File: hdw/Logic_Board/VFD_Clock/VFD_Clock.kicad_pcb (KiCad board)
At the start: 4 copper layers, 200 x 50 mm, 488 parts, among them J1601 Prog, J201 Power Input, J701 USB_B_Micro, Q1001 2N7002, Q1002 2N7002, Q1003 2N7002, Q1101 PMSTA06, Q1102 PMSTA06, Q1103 BC856W, Q1104 BC856W, Q1105 PMSTA06, Q1106 PMSTA06, Q1107 BC856W, Q1108 BC856W, Q1109 PMSTA06, Q1110 PMSTA06, Q1111 BC856W, Q1112 BC856W, Q1113 PMSTA06, Q1114 PMSTA06, Q1115 BC856W, Q1116 BC856W, Q1201 PMSTA06, Q1202 PMSTA06, Q1203 BC856W, Q1204 BC856W, Q1205 PMSTA06, Q1206 PMSTA06, Q1207 BC856W, Q1208 BC856W, Q1209 PMSTA06, Q1210 PMSTA06, Q1211 BC856W, Q1212 BC856W, Q1701 2N7002, Q201 Si2319CDS, Q202 PMT560ENEA, Q501 IRFL214TRPBF, SW1306 Select, U1001 TPS22929D, U1002 PCA9536DP, U1302 74LVC2G14, U1303 74LVC1G79, U1305 MAX6816, U1601 TL331, U1602 74LVC1G86, U1701 LTC3128-UFD, U1702 LTC4419DD, U1703 LTC3221, U1801 AT24CS01-STUM, U1901 74LVC1G38, U1902 74LVC1G38, U2001 OPT3001, U201 CDCS503, U202 LTC2946DE, U203 TPS2411PWR, U2101 MCP9700AT-HLT, U2102 MCP9700AT-HLT, U2103 MCP9700AT-HLT, U2104 MCP9700AT-HLT, U2201 74LVC1G08, U2202 DS1683, U2203 74LVC1G38, U2401 STWD100YNWWY3F, U2402 74LVC2G74, U301 PIC18LF67K40-I_PT, U401 LT8643S, U501 LT6700-1-S6, U502 LT3757, U601 TPS62150, U701 74LVC1G17, U702 TPD3S014DBVR, U703 FT234XD, U801 74LVC1G38, U802 74LVC1G38, U803 74LVC1G38, U804 74LVC1G38, U805 74LVC1G38, U806 74LVC1G240, U901 ISO7331C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

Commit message: Few fixes, added BLE
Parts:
- removed A1001: 0x41, Oddities:Dummy_Empty
- removed A1801: 0x50/0x58(UID), Oddities:Dummy_Empty
- removed A2001: 0x44, Oddities:Dummy_Empty
- removed A201: 0x6F, Oddities:Dummy_Empty
- removed A2201: 0x6B, Oddities:Dummy_Empty
- removed A301: MASTER, Oddities:Dummy_Empty
- removed BZ1001: AI-1027-TWT-3V-R, Custom Footprints Library:AI-1027-TWT-3V-R
- removed C1303, C1306, C1307, C1401, C1402, C1403, C1404, C1710, C1711, C305, C706, C707: 0.1uF, Capacitors_SMD:C_0603
- removed C1304, C1305, C1707: 2.2uF, Capacitors_SMD:C_0805
- removed C1708: 1uF, Capacitors_SMD:C_0603
- removed C1709: 4.7uF, Capacitors_SMD:C_0603
- removed C207: 2200pF, Capacitors_SMD:C_0603
- removed C208: 100pF, Capacitors_SMD:C_0603
- removed C209, C510: 47uF, Capacitors_Tantalum_SMD:CP_Tantalum_Case-X_EIA-7343-43_Reflow
- removed C2205, C2206: 10uF, Capacitors_SMD:C_1206
- removed C304, C307: 1nF, Capacitors_SMD:C_0603
- removed C306, C407, C710: 10nF, Capacitors_SMD:C_0603
- removed C308, C309: 9pF, Capacitors_SMD:C_0603
- removed C408: 1uF, Capacitors_SMD:C_0805
- removed C409: 4.7pF, Capacitors_SMD:C_0603
- removed C410: 100uF, Capacitors_SMD:C_1206
- removed C411: 220uF, Capacitors_Tantalum_SMD:CP_Tantalum_Case-X_EIA-7343-43_Reflow
- removed C506: 6.8nF, Capacitors_SMD:C_0603
- removed C507: 4.7uF, Capacitors_SMD:C_0805
- removed C508: 1uF, Capacitors_SMD:C_1210
- removed C509, C511: 0.1uF, Capacitors_SMD:C_0805
- removed C708, C709: 47pF, Capacitors_SMD:C_0603
- removed D1002: Orange, LEDs:LED_0603
- removed D1003, D1008, D1009, D806: Red, LEDs:LED_0603
- removed D1004, D1005, D1006: Blue, LEDs:LED_0603
- removed D1007, D801, D802, D803, D804, D805: Green, LEDs:LED_0603
- removed D1901, D1903: Green, LEDs:LED_D3.0mm_Horizontal_O3.81mm_Z10.0mm
- removed D1902, D1904: Green, LEDs:LED_D3.0mm_Horizontal_O1.27mm_Z2.0mm
- removed D2201: 1N5819, Diodes_SMD:D_SOD-123F
- removed D501: SMD1200PL-TP‎, Diodes_SMD:D_SOD-123
- removed D702: Yellow, LEDs:LED_0603
- removed F201: C1Q 2, Fuse_Holders_and_Fuses:Fuse_SMD1206_Reflow
- removed FB401: 100, Inductors_SMD:L_1812
- removed FID2301, FID2302, FID2303: TP, Fiducials:Fiducial_0.5mm_Dia_1mm_Outer
- removed G*** (x2): Microchip_Logo, Custom Footprints Library:Microchip_Logo
- removed J1601: Prog, Custom Footprints Library:PICKIT3_Header
- removed J701: USB_B_Micro, Connectors_USB:USB_Micro-B_Wuerth-629105150521_CircularHoles
- removed L501: 560uH, Inductors_SMD:L_Wuerth_WE-PD-Typ-LS
- removed L701: 600R 0.5A, Inductors_SMD:L_0603
- removed MH2301, MH2302, MH2303, MH2304, MH2305, MH2306, MH2307, MH2308: 4-40 Mounting Hole, Mounting_Holes:MountingHole_3mm
- removed MK2301, MK2302, MK2303, MK2304, MK2305, MK2306, MK2307, MK2308: #4-40 Screw, Oddities:Dummy_Empty
- removed MK2309, MK2310, MK2311, MK2312, MK2313, MK2314, MK2315, MK2316: #4-40 Standoff, Oddities:Dummy_Empty
- removed Q1002, Q1003, Q1701: 2N7002, TO_SOT_Packages_SMD:SOT-23
- removed Q1101, Q1102, Q1105, Q1106, Q1109, Q1110, Q1113, Q1114, Q1201, Q1202, Q1205, Q1206, Q1209, Q1210: PMSTA06, TO_SOT_Packages_SMD:SOT-323_SC-70
- removed Q1103, Q1104, Q1107, Q1108, Q1111, Q1112, Q1115, Q1116, Q1203, Q1204, Q1207, Q1208, Q1211, Q1212: BC856W, TO_SOT_Packages_SMD:SOT-323_SC-70
- removed Q501: IRFL214TRPBF, TO_SOT_Packages_SMD:SOT-223-3_TabPin2
- removed R1101, R1102, R1109, R1110, R1117, R1118, R1125, R1126, R1217, R1218, R1402, R1404, R1406, R1601, R1602, R1603, R1605, R1901, R1902, R1907, R1908, R2206, R303, R304, R305, R504, R506, R511, R701, R901, R902, R903, R904, R905, R906: 10k, Resistors_SMD:R_0603
- removed R1103, R1105, R1111, R1113, R1119, R1121, R1127, R1129, R1211, R1213, R1219, R1221: 220k, Resistors_SMD:R_0603
- removed R1104, R1106, R1112, R1114, R1120, R1122, R1128, R1130, R1212, R1214, R1220, R1222: 68k, Resistors_SMD:R_0603
- removed R1107, R1108, R1115, R1116, R1123, R1124, R1131, R1132, R1215, R1216, R1223, R1224, R1401, R1403, R1405, R1407: 100k, Resistors_SMD:R_0603
- removed R1408, R1903, R1904, R1905, R1906, R704, R811, R812: 1k, Resistors_SMD:R_0603
- removed R1604, R1708, R301, R302: 0, Resistors_SMD:R_0603
- removed R1706: 3.65k, Resistors_SMD:R_0603
- removed R1707: 340k, Resistors_SMD:R_0603
- removed R1709, R1712, R1713: 1M, Resistors_SMD:R_0603
- removed R1710: 324k, Resistors_SMD:R_0603
- removed R1711: 276k, Resistors_SMD:R_0603
- removed R501: 196k, Resistors_SMD:R_0603
- removed R502: 237, Resistors_SMD:R_0603
- removed R503: 1.2k, Resistors_SMD:R_0603
- removed R505: 10.5k, Resistors_SMD:R_0603
- removed R507: 22k, Resistors_SMD:R_0603
- removed R508: 2, Resistors_SMD:R_0603
- removed R509: 0.51, Resistors_SMD:R_1206
- removed R510: 356k, Resistors_SMD:R_0603
- removed R702, R703: 27, Resistors_SMD:R_0603
- removed REF**: Symbol_HighVoltage_Type2_Silkscreen_VerySmall, Custom Footprints Library:Symbol_HighVoltage_Type2_Silkscreen_VerySmall
- removed REF**: Symbol_Barrel_Polarity, Symbols:Symbol_Barrel_Polarity
- removed REF**: Symbol_Highvoltage_Type2_Silkscreen_Small, Custom Footprints Library:Symbol_Highvoltage_Type2_Silkscreen_Small
- removed REF***: KiCad-Logo_8mm_SilkScreen, Symbols:KiCad-Logo_8mm_SilkScreen
- removed REF***: OSHW-Logo2_14.6x12mm_SilkScreen, Symbols:OSHW-Logo2_14.6x12mm_SilkScreen
- removed REF***: ESD-Logo_13.2x12mm_SilkScreen, Symbols:ESD-Logo_13.2x12mm_SilkScreen
- removed SW1306: Select, Custom Footprints Library:ACZ11BR4E-15FA1-20C
- removed TP1301, TP1303: Date, Wire_Pads:SolderWirePad_single_SMD_5x10mm
- removed TP1302: Time, Wire_Pads:SolderWirePad_single_SMD_5x10mm
- removed TP1304: Alarm, Wire_Pads:SolderWirePad_single_SMD_5x10mm
- removed TP1305: Brightness, Wire_Pads:SolderWirePad_single_SMD_5x10mm
- removed TP1701, TP1702, TP501, TP701: TP, Measurement_Points:Measurement_Point_Round-SMD-Pad_Small
- removed TP301: I2C, Pin_Headers:Pin_Header_Straight_1x03_Pitch2.54mm
- removed TP302: USB_UART, Pin_Headers:Pin_Header_Straight_1x03_Pitch2.54mm
- removed TP702: TP, Pin_Headers:Pin_Header_Straight_1x01_Pitch2.54mm
- removed U1302: 74LVC2G14, TO_SOT_Packages_SMD:SOT-363_SC-70-6
- removed U1303: 74LVC1G79, TO_SOT_Packages_SMD:SOT-353_SC-70-5
- removed U1305: MAX6816, TO_SOT_Packages_SMD:SOT-143
- removed U1601: TL331, TO_SOT_Packages_SMD:SOT-23-5
- removed U1602: 74LVC1G86, TO_SOT_Packages_SMD:SOT-353_SC-70-5
- removed U1701: LTC3128-UFD, Housings_DFN_QFN:QFN-20-1EP_4x5mm_Pitch0.5mm
- removed U1702: LTC4419DD, Housings_DFN_QFN:DFN-10-1EP_3x3mm_Pitch0.5mm
- removed U1703: LTC3221, Housings_DFN_QFN:DFN-6-1EP_2x2mm_Pitch0.5mm
- removed U1902, U2203, U802, U803, U804, U805: 74LVC1G38, TO_SOT_Packages_SMD:SOT-353_SC-70-5
- removed U202: LTC2946DE, Housings_DFN_QFN:DFN-16-1EP_3x4mm_Pitch0.45mm
- removed U203: TPS2411PWR, Housings_SSOP:TSSOP-14_4.4x5mm_Pitch0.65mm
- removed U2202: DS1683, Housings_SOIC:SOIC-8_3.9x4.9mm_Pitch1.27mm
- removed U806: 74LVC1G240, TO_SOT_Packages_SMD:SOT-353_SC-70-5
- removed VFD0, VFD1, VFD2, VFD3, VFD4, VFD5: IV-6, VFD:IV-6
- removed Y301: 32.768kHz, Crystals:Crystal_SMD_2012-2pin_2.0x1.2mm
- removed Z1402, Z1403: BZT52C3V3S, Diodes_SMD:D_SOD-323
- removed Z1601: BZT52C5V6S, Diodes_SMD:D_SOD-323
- removed Z201: MMSZ5240BS, Diodes_SMD:D_SOD-323
- added BT1201: BR-2/3AE5SPN, Custom Footprints Library:BR-2_3AE5SPN, F.Cu at (326.2, 31.5)
- added BT1202: CR2032, Battery_Holders:Keystone_1058_1x2032-CoinCell, F.Cu at (362.1, 34.7)
- added BT1203: TLH-5935/P, Custom Footprints Library:TLH-5935, F.Cu at (342.5, 0.76)
- added BZ1801: CST-931RP-A, Buzzer_Beeper:MagneticBuzzer_CUI_CST-931RP-A, F.Cu at (432.5, 11.6)
- added C1003: 0.1uF, Capacitors_SMD:C_0603, F.Cu at (334.2, 82.3)
- added C1004: 0.1uF, Capacitors_SMD:C_0603, F.Cu at (319.2, 94.4)
- added C1005: 0.1uF, Capacitors_SMD:C_0603, F.Cu at (323.4, 92.7)
- added C1006: 10nF, Capacitors_SMD:C_0603, F.Cu at (319.2, 96.8)
- added C1007: 6.8nF, Capacitors_SMD:C_0603, F.Cu at (338.7, 79.5)
- added C1008: 1nF, Capacitors_SMD:C_0603, F.Cu at (327.5, 91.5)
- added C1009: 4.7uF, Capacitors_SMD:C_0805, F.Cu at (315.0, 96.3)
- added C1010: 1uF, Capacitors_SMD:C_1210, F.Cu at (329.5, 80.4)
- added C1011: 0.1uF, Capacitors_SMD:C_0805, F.Cu at (334.5, 79.8)
- added C1101: 0.1uF, Capacitors_SMD:C_0603, F.Cu at (449.8, 83.0)
- added C1102: 0.1uF, Capacitors_SMD:C_0603, F.Cu at (460.4, 78.3)
- added C1103: 0.1uF, Capacitors_SMD:C_0603, F.Cu at (460.0, 83.0)
- added C1104: 0.1uF, Capacitors_SMD:C_0603, F.Cu at (460.4, 80.6)
- added C1201: 10uF, Capacitors_SMD:C_1206, F.Cu at (310.0, 42.2)
- added C1202: 10uF, Capacitors_SMD:C_1206, F.Cu at (310.0, 48.6)
- added C1203: 10uF, Capacitors_SMD:C_1206, F.Cu at (315.5, 42.2)
- added C1204: 10uF, Capacitors_SMD:C_1206, F.Cu at (310.0, 45.3)
- added C1205: 0.1uF, Capacitors_SMD:C_0603, F.Cu at (381.0, 11.1)
- added C1206: 10uF, Capacitors_SMD:C_1206, F.Cu at (379.2, 8.38)
- added C1207: 10uF, Capacitors_SMD:C_1206, F.Cu at (315.5, 45.3)
- added C1501: 0.1uF, Capacitors_SMD:C_0603, F.Cu at (414.5, 181.9)
- added C1502: 0.1uF, Capacitors_SMD:C_0603, B.Cu at (420.0, 193.4)
- added C1604: 10nF, Capacitors_SMD:C_0603, F.Cu at (640.9, 148.3)
- added C1605: 10nF, Capacitors_SMD:C_0603, F.Cu at (645.2, 148.3)
- added C1606: 1nF, Capacitors_SMD:C_0603, F.Cu at (640.9, 146.9)
- added C1607: 1nF, Capacitors_SMD:C_0603, F.Cu at (645.2, 146.9)
- added C1608: 0.1uF, Capacitors_SMD:C_0603, F.Cu at (654.6, 130.4)
- added C1609: 0.1uF, Capacitors_SMD:C_0603, F.Cu at (643.7, 123.4)
- added C1610: 10uF, Capacitors_SMD:C_0603, F.Cu at (656.0, 130.4)
- added C1611: 10nF, Capacitors_SMD:C_0603, F.Cu at (653.2, 130.4)
- added C1612: 10nF, Capacitors_SMD:C_0603, F.Cu at (643.7, 124.8)
- added C1613: 1nF, Capacitors_SMD:C_0603, F.Cu at (651.8, 130.4)
- added C1614: 1nF, Capacitors_SMD:C_0603, F.Cu at (643.7, 126.2)
- added C1615: 0.1uF, Capacitors_SMD:C_0603, F.Cu at (639.3, 123.4)
- added C1616: 0.1uF, Capacitors_SMD:C_0603, F.Cu at (654.6, 136.8)
- added C1617: 10uF, Capacitors_SMD:C_0603, F.Cu at (639.3, 122.0)
- added C1618: 10nF, Capacitors_SMD:C_0603, F.Cu at (639.3, 124.8)
- added C1619: 10nF, Capacitors_SMD:C_0603, F.Cu at (653.2, 136.8)
- added C1620: 1nF, Capacitors_SMD:C_0603, F.Cu at (639.3, 126.2)
- added C1621: 1nF, Capacitors_SMD:C_0603, F.Cu at (651.8, 136.8)
- added C1622: 0.1uF, Capacitors_SMD:C_0603, F.Cu at (628.3, 136.9)
- added C1623: 0.1uF, Capacitors_SMD:C_0603, F.Cu at (637.7, 149.7)
- added C1624: 10uF, Capacitors_SMD:C_0603, F.Cu at (626.9, 136.9)
- added C1625: 10nF, Capacitors_SMD:C_0603, F.Cu at (629.7, 136.9)
- added C1626: 10nF, Capacitors_SMD:C_0603, F.Cu at (637.7, 148.3)
- added C1627: 1nF, Capacitors_SMD:C_0603, F.Cu at (631.1, 136.9)
- added C1628: 1nF, Capacitors_SMD:C_0603, F.Cu at (637.7, 146.9)
- added C1802: 0.1uF, Capacitors_SMD:C_0603, F.Cu at (454.2, 7.98)
- added C1803: 0.1uF, Capacitors_SMD:C_0603, F.Cu at (441.4, 21.0)
- added C1804: 0.1uF, Capacitors_SMD:C_0603, F.Cu at (445.4, 17.7)
- added C2002: 0.1uF, Capacitors_SMD:C_0603, F.Cu at (398.1, 63.4)
- added C2003: 0.1uF, Capacitors_SMD:C_0603, F.Cu at (406.7, 54.8)
- added C2004: 0.1uF, Capacitors_SMD:C_0603, F.Cu at (390.3, 67.2)
- added C2005: 0.1uF, Capacitors_SMD:C_0603, F.Cu at (398.5, 59.5)
- added C2006: 0.1uF, Capacitors_SMD:C_0603, F.Cu at (394.2, 63.4)
- added C2007: 0.1uF, Capacitors_SMD:C_0603, F.Cu at (402.7, 57.2)
- added C205: 100uF, Capacitors_Tantalum_SMD:CP_Tantalum_Case-X_EIA-7343-43_Reflow, F.Cu at (329.6, 56.7)
- added C2301: 10uF, Capacitors_SMD:C_0603, B.Cu at (599.6, 94.9)
- added C2302: 10uF, Capacitors_SMD:C_0603, B.Cu at (598.2, 94.9)
- added C2303: 10uF, Capacitors_SMD:C_0603, B.Cu at (596.8, 94.9)
- added C2304: 0.1uF, Capacitors_SMD:C_0603, B.Cu at (601.0, 94.9)
- added C2403: 0.1uF, Capacitors_SMD:C_0603, F.Cu at (405.9, 38.7)
- added C2404: 0.1uF, Capacitors_SMD:C_0603, F.Cu at (412.4, 33.6)
- added C2405: 4.7uF, Capacitors_SMD:C_0805, F.Cu at (401.2, 41.2)
- added C2406: 0.1uF, Capacitors_SMD:C_0603, F.Cu at (412.4, 31.3)
- added C2407: 0.1uF, Capacitors_SMD:C_0603, F.Cu at (409.9, 36.0)
- added C2408: 47pF, Capacitors_SMD:C_0603, F.Cu at (416.3, 31.3)
- added C2409: 47pF, Capacitors_SMD:C_0603, F.Cu at (405.4, 41.0)
- added C2410: 0.1uF, Capacitors_SMD:C_0603, F.Cu at (400.9, 46.1)
- added C2501: 0.1uF, Capacitors_SMD:C_0603, B.Cu at (503.6, 161.3)
- added C2502: 0.1uF, Capacitors_SMD:C_0603, B.Cu at (503.6, 169.9)
- added C2503: 0.56uF, Capacitors_SMD:C_2220, B.Cu at (506.0, 165.6)
- added C2504: 0.1uF, Capacitors_SMD:C_0603, B.Cu at (508.5, 161.3)
- added C2505: 0.1uF, Capacitors_SMD:C_0603, B.Cu at (508.5, 169.9)
- added C2506: 0.1uF, Capacitors_SMD:C_0603, B.Cu at (512.1, 174.0)
- added C2601: 0.1uF, Capacitors_SMD:C_0603, F.Cu at (392.8, 26.8)
- added C2602: 0.1uF, Capacitors_SMD:C_0603, F.Cu at (400.5, 27.8)
- added C2603: 0.1uF, Capacitors_SMD:C_0603, F.Cu at (396.6, 27.8)
- added C2701: 10uF, Capacitors_SMD:C_0603, F.Cu at (604.8, 133.5)
- added C2702: 0.1uF, Capacitors_SMD:C_0603, F.Cu at (606.3, 133.5)
- added C2703: 0.1uF, Capacitors_SMD:C_0603, F.Cu at (606.2, 136.7)
- added C2704: 0.1uF, Capacitors_SMD:C_0603, F.Cu at (597.5, 144.7)
- added C2801: 0.1uF, Capacitors_SMD:C_0603, B.Cu at (562.1, 188.9)
- added C2802: 0.1uF, Capacitors_SMD:C_0603, B.Cu at (569.0, 188.9)
- added C2803: 10nF, Capacitors_SMD:C_0603, F.Cu at (562.1, 188.9)
- added C2804: 10nF, Capacitors_SMD:C_0603, F.Cu at (569.0, 188.9)
- added C2805: 1nF, Capacitors_SMD:C_0603, F.Cu at (562.1, 190.3)
- added C2806: 1nF, Capacitors_SMD:C_0603, F.Cu at (569.0, 190.3)
- added C2901: 0.1uF, Capacitors_SMD:C_0603, B.Cu at (542.2, 209.0)
- added C2902: 10nF, Capacitors_SMD:C_0603, F.Cu at (542.2, 209.0)
- added C2903: 1nF, Capacitors_SMD:C_0603, F.Cu at (542.2, 210.4)
- added C2904: 0.1uF, Capacitors_SMD:C_0603, B.Cu at (507.5, 220.6)
- added C2905: 4.7uF, Capacitors_SMD:C_0805, B.Cu at (509.1, 220.6)
- added C2906: 0.1uF, Capacitors_SMD:C_0603, B.Cu at (512.7, 220.6)
- added C2907: 4.7uF, Capacitors_SMD:C_0805, B.Cu at (511.0, 220.6)
- added C301: 0.1uF, Capacitors_SMD:C_0603, F.Cu at (457.5, 94.3)
- added C604: 22uF, Capacitors_SMD:C_1206, F.Cu at (356.4, 96.1)
- added C605: 22uF, Capacitors_SMD:C_1206, F.Cu at (348.0, 105.9)
- added C606: 0.1uF, Capacitors_SMD:C_0603, F.Cu at (365.1, 95.7)
- added C904: 0.1uF, Capacitors_SMD:C_0603, F.Cu at (440.1, 99.7)
- added C905: 0.1uF, Capacitors_SMD:C_0603, F.Cu at (434.8, 106.7)
- added D1801: MBR0580, Diode_SMD:D_SOD-123, F.Cu at (440.6, 18.2)
- added D2001: Green, LEDs:LED_0603, F.Cu at (402.8, 54.8)
- added D2002: Red, LEDs:LED_0603, F.Cu at (390.3, 64.9)
- added D2003: Red, LEDs:LED_0603, F.Cu at (394.6, 61.0)
- added D2004: Red, LEDs:LED_0603, F.Cu at (398.8, 57.2)
- added D2005: Red, LEDs:LED_0603, F.Cu at (398.8, 54.8)
- added D2006: Red, LEDs:LED_0603, F.Cu at (394.6, 58.7)
- added D2007: Red, LEDs:LED_0603, F.Cu at (390.3, 62.5)
- added D201: 24V, Diodes_SMD:D_SMA, F.Cu at (328.3, 62.0)
- added D2101: Green, LEDs:LED_0603, F.Cu at (394.3, 85.2)
- added D2102: Green, LEDs:LED_0603, F.Cu at (403.1, 73.6)
- added D2103: Green, LEDs:LED_0603, F.Cu at (398.8, 78.3)
- added D2104: Green, LEDs:LED_0603, F.Cu at (390.3, 85.2)
- added D2105: Green, LEDs:LED_0603, F.Cu at (399.1, 76.0)
- added D2106: Red, LEDs:LED_0603, F.Cu at (394.6, 81.3)
- added D2107: Green, LEDs:LED_0603, F.Cu at (399.1, 73.6)
- added D2301: MBR0530, Diode_SMD:D_SOD-123, B.Cu at (594.9, 95.8)
- added D2401: Yellow, LEDs:LED_0603, F.Cu at (406.0, 36.3)
- added D2701: Red, LEDs:LED_0603, F.Cu at (607.6, 139.8)
- added D2702: Yellow, LEDs:LED_0603, F.Cu at (600.8, 143.3)
- added H3101: MountingHole, MountingHole:MountingHole_3mm_Pad_Via, F.Cu at (38.3, 70.3)
- added H3102: MountingHole, MountingHole:MountingHole_3mm_Pad_Via, F.Cu at (38.3, 112.3)
- added H3103: MountingHole, MountingHole:MountingHole_3mm_Pad_Via, F.Cu at (102.3, 70.3)
- added H3104: MountingHole, MountingHole:MountingHole_3mm_Pad_Via, F.Cu at (102.3, 112.3)
- added H3105: MountingHole, MountingHole:MountingHole_3mm_Pad_Via, F.Cu at (166.3, 70.3)
- added H3106: MountingHole, MountingHole:MountingHole_3mm_Pad_Via, F.Cu at (166.3, 112.3)
- added H3107: MountingHole, MountingHole:MountingHole_3mm_Pad_Via, F.Cu at (230.3, 70.3)
- added H3108: MountingHole, MountingHole:MountingHole_3mm_Pad_Via, F.Cu at (230.3, 112.3)
- added J1501: PICKIT3, Custom Footprints Library:PICKIT3_Header, F.Cu at (417.3, 172.9)
- added J1801: I2C, Pin_Headers:Pin_Header_Straight_1x03_Pitch2.54mm, F.Cu at (444.7, 9.13)
- added J1802: USB UART, Pin_Headers:Pin_Header_Straight_1x03_Pitch2.54mm, F.Cu at (440.1, 9.13)
- added J1803: BLE UART, Pin_Headers:Pin_Header_Straight_1x03_Pitch2.54mm, F.Cu at (586.6, 131.8)
- added J2401: USB_B_Mini, Connectors:USB_Mini-B, F.Cu at (394.2, 41.0)
- added J3001: DSP_IO_Connector, Connector_Samtec:Samtec_LSHM-130-xx.x-x-DV-N_2x30_P0.50mm_Vertical, F.Cu at (242.5, 90.2)
- added L1001: 100uH, Inductors_SMD:L_Vishay_IHLP-4040, F.Cu at (314.1, 84.2)
- added L1201: 2.2uH, Inductors_SMD:L_Vishay_IHLP-1212, F.Cu at (373.6, 9.13)
- added L1601: 600R 0.5A, Inductors_SMD:L_0603, F.Cu at (636.8, 151.8)
- added L1602: 600R 0.5A, Inductors_SMD:L_0603, F.Cu at (638.6, 151.8)
- added L1702: 600R 0.5A, Inductors_SMD:L_0603, F.Cu at (655.6, 122.8)
- added L2401: 600R 0.5A, Inductors_SMD:L_0603, F.Cu at (416.2, 33.8)
- added L2402: 600R 0.5A, Inductors_SMD:L_0603, F.Cu at (409.8, 38.5)
- added L801: 2.2u, Inductors_SMD:L_Vishay_IHLP-2020, F.Cu at (427.6, 33.4)
- added Q1301: BSS214NW, TO_SOT_Packages_SMD:SOT-323_SC-70, F.Cu at (382.1, 104.5)
- added Q1302: IRLML2060, Package_TO_SOT_SMD:SOT-23, F.Cu at (386.6, 96.8)
- added Q1303: BSS214NW, TO_SOT_Packages_SMD:SOT-323_SC-70, F.Cu at (382.1, 100.9)
- added Q1304: BSS214NW, TO_SOT_Packages_SMD:SOT-323_SC-70, F.Cu at (386.6, 100.9)
- added Q1305: TP0610T, Package_TO_SOT_SMD:SOT-23, F.Cu at (377.7, 105.9)
- added Q1306: IRLML2060, Package_TO_SOT_SMD:SOT-23, F.Cu at (382.1, 96.8)
- added Q1307: BSS214NW, TO_SOT_Packages_SMD:SOT-323_SC-70, F.Cu at (391.0, 96.3)
- added Q1308: IRLML2060, Package_TO_SOT_SMD:SOT-23, F.Cu at (377.7, 101.3)
- added Q1309: BSS214NW, TO_SOT_Packages_SMD:SOT-323_SC-70, F.Cu at (386.6, 104.5)
- added Q1310: TP0610T, Package_TO_SOT_SMD:SOT-23, F.Cu at (377.7, 96.8)
- added Q1501: BSS214NW, TO_SOT_Packages_SMD:SOT-323_SC-70, F.Cu at (417.4, 193.4)
- added Q1801: BSS214NW, TO_SOT_Packages_SMD:SOT-323_SC-70, F.Cu at (449.3, 12.3)
- added Q2701: BSS214NW, TO_SOT_Packages_SMD:SOT-323_SC-70, F.Cu at (601.6, 139.6)
- added R1307: 10k, Resistors_SMD:R_0603, F.Cu at (390.6, 99.4)
- added R1315: 10k, Resistors_SMD:R_0603, F.Cu at (394.1, 103.2)
- added R1501: 10, Resistors_SMD:R_0603, F.Cu at (414.8, 193.4)
- added R1502: 10k, Resistors_SMD:R_0603, B.Cu at (416.4, 193.4)
- added R1503: 100, Resistors_SMD:R_0603, F.Cu at (420.0, 193.4)
- added R1504: 10k, Resistors_SMD:R_0603, B.Cu at (421.6, 193.4)
- added R1505: 1k, Resistors_SMD:R_0603, F.Cu at (421.6, 193.4)
- added R1807: 10k, Resistors_SMD:R_0603, F.Cu at (452.7, 15.3)
- added R2006: 10k, Resistors_SMD:R_0603, F.Cu at (408.9, 62.3)
- added R2007: 1k, Resistors_SMD:R_0603, F.Cu at (401.8, 62.1)
- added R2008: 1k, Resistors_SMD:R_0603, F.Cu at (405.3, 64.7)
- added R2009: 10k, Resistors_SMD:R_0603, F.Cu at (409.3, 59.9)
- added R2010: 10k, Resistors_SMD:R_0603, F.Cu at (405.3, 62.2)
- added R2011: 1k, Resistors_SMD:R_0603, F.Cu at (406.4, 57.2)
- added R2012: 1k, Resistors_SMD:R_0603, F.Cu at (394.0, 68.1)
- added R2013: 10k, Resistors_SMD:R_0603, F.Cu at (397.9, 65.8)
- added R2014: 1k, Resistors_SMD:R_0603, F.Cu at (410.4, 54.9)
- added R2105: 1k, Resistors_SMD:R_0603, F.Cu at (401.9, 83.7)
- added R2106: 1k, Resistors_SMD:R_0603, F.Cu at (406.0, 80.9)
- added R2107: 1k, Resistors_SMD:R_0603, F.Cu at (401.6, 86.2)
- added R2404: 40.2k, Resistors_SMD:R_0603, F.Cu at (413.4, 38.4)
- added R2405: 10k, Resistors_SMD:R_0603, F.Cu at (412.0, 43.5)
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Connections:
- C1001 pad 1: +3V3 -> Net-(C1001-Pad1)
- C1002 pad 1: +3V3 -> Net-(C1001-Pad1)
- C1601 pad 1: Net-(C1601-Pad1) -> +3.3V_BCKP
- C1602 pad 1: +24V -> +3.3V_BCKP
- C1603 pad 1: +3V3 -> +3.3V_BCKP
- C1701 pad 1: +3V3 -> Net-(C1701-Pad1)
- C1703 pad 1: VHU -> Net-(C1701-Pad1)
- C1703 pad 2: MID -> GND
- C1704 pad 1: MID -> Net-(C1702-Pad1)
- C1705 pad 1: Net-(C1705-Pad1) -> Net-(C1701-Pad1)
- C1706 pad 1: Net-(C1706-Pad1) -> Net-(C1702-Pad1)
- C1901 pad 1: +3V3 -> VBAT
- C201 pad 1: +3V3 -> +12Vin
- C202 pad 1: +3V3 -> +12Vin
- C203 pad 1: +3V3 -> +12Vin
- C2101 pad 1: +3V3 -> +12V
- C2102 pad 1: +3V3 -> Net-(C2102-Pad1)
- C2103 pad 1: Ambient_Temp -> +3V3
- C2104 pad 1: VFF_Temp -> +3V3
- C2105 pad 1: +3V3 -> +5V_USB
- C2105 pad 2: GND -> GND_USB
- C2107 pad 1: POS3P3_TEMP -> +3V3
- C2108 pad 1: VAN_Temp -> +3V3
- C2201 pad 1: +3V3 -> +3.3V_BCKP
- C2202 pad 1: Net-(C2202-Pad1) -> +3.3V_BCKP
- C2204 pad 1: Net-(C2202-Pad1) -> +3V3
- C2401 pad 1: +3V3 -> Net-(C2401-Pad1)
- C2401 pad 2: GND -> GND_USB
- C2402 pad 1: +3V3 -> +5V_USB
- C2402 pad 2: GND -> GND_USB
- C302 pad 1: +3.3V_MNG -> +3V3
- C303 pad 1: +3.3V_MNG -> +3V3
- C401 pad 1: +24V -> Net-(C401-Pad1)
- C403 pad 1: Net-(C403-Pad1) -> Net-(C401-Pad1)
- C405 pad 1: Net-(C403-Pad1) -> Net-(C404-Pad1)
- C406 pad 1: Net-(C403-Pad1) -> +3V3
- C501 pad 1: +24V -> POS3P3_SNS_IN+
- C501 pad 2: GND -> POS3P3_SNS_IN-
- C504 pad 1: +3V3 -> POS3P3_SNS_OUT+
- C504 pad 2: GND -> POS3P3_SNS_OUT-
- C505 pad 1: Net-(C505-Pad1) -> +3V3
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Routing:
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- removed copper zone on F.Cu, net +24V
- removed copper zone on B.Cu, net +3.3V_MNG
- removed copper zone on B.Cu, net +3V3
- removed copper zone on F.Cu, net +3V3
- removed copper zone on Power_Plane, net +3V3
- removed copper zone on F.Cu, net +5V_USB
- removed copper zone on Power_Plane, net +5V_USB
- removed copper zone on GND_Plane, net GND
- removed copper zone on F.Cu, net GND_USB
- removed copper zone on GND_Plane, net GND_USB
- removed copper zone on F.Cu, net Net-(C1702-Pad1)
- removed copper zone on B.Cu, net Net-(C1706-Pad1)
- removed copper zone on F.Cu, net Net-(C1706-Pad1)
- removed copper zone on F.Cu, net Net-(C207-Pad1)
- removed copper zone on B.Cu, net Net-(C403-Pad1)
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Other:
- net class Default: clearance 0.2032 -> 0.127; trace_width 0.2032 -> 0.127; via_dia 0.6 -> 0.56; via_drill 0.4 -> 0.2
- net class Power: clearance 0.2032 -> 0.127; via_dia 0.6 -> 0.56; via_drill 0.4 -> 0.2
- net class Power_HV removed
- net class Signal: clearance 0.2032 -> 0.127; trace_width 0.2032 -> 0.127; via_dia 0.6 -> 0.56; via_drill 0.4 -> 0.2
- net class Signal_HV removed
- rule pad_to_mask_clearance: 0.2 -> 0.051
- rule trace_clearance: 0.2032 -> 0.127
- rule trace_min: 0.2032 -> 0.0508
- rule via_min_drill: 0.3 -> 0.199898
- board text added: "BLE Active"
- board text added: "BLE Enable"
- board text removed: "+"
- board text removed: "+24V"
- board text removed: "+24V PGOOD"
- board text removed: "+3.3V"
- board text removed: "+3.3V MNG"
- board text removed: "+3.3V PGOOD"
- board text removed: "+5V USB"
- board text removed: "-"
- board text removed: "0"
- board text removed: "1"
- board text removed: "2"
- board text removed: "3"
- board text removed: "4"
- board text removed: "5"
- board text removed: "ALARM"
- board text removed: "BRIGHTNESS"
- board text removed: "COM"
- board text removed: "DATE"
- board text removed: "GND"
- board text removed: "GND USB"
- board text removed: "HU PGOOD"
- board text removed: "I2C"
- board text removed: "PICKIT3"
- board text removed: "POWER"
- board text removed: "PROG"
- board text removed: "PWR ERR ALRM ON ALRM ST DATE ST TIME ST COM ERR HRTBT"
- board text removed: "RESET"
- board text removed: "REV A Fall 2018"
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
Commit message: Arranged more parts on PCB
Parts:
- added C1105: 0.1uF, Capacitors_SMD:C_0805, F.Cu at (560.5, 182.8)
- C1101, C1102, C1103, C2201, C2202, C2203, C2204, C2401, C2402, C2404, C2405, C2407, C2408, C2409, C301, C302, C303, C501, C502, C503, C504, C505, C701, C702, C703, C704, C705, C901, C902, C903, C904, C905, R2201, R2202, R2204, R2205, R2401, R2408, R2409, U1101, U1102, U2402, U301, U302, U501, U502, U503, U701, U702, U703, U901, U902, U903: moved to B.Cu
- moved U1001 275.0 mm to (559.1, 187.3), turned to 270 degrees
- moved Q1001 265.3 mm to (541.2, 195.5), turned to 180 degrees
- moved C1004 262.2 mm to (564.5, 187.3), turned to 90 degrees
- moved C1006 260.1 mm to (563.1, 187.3), turned to 90 degrees
- moved R1013 257.2 mm to (550.9, 186.6), turned to 270 degrees
- moved U1002 254.2 mm to (552.4, 194.9), turned to 180 degrees
- moved R1007 253.9 mm to (557.1, 193.2)
- moved C1009 253.8 mm to (547.1, 199.3), turned to 270 degrees
- moved C1008 253.0 mm to (561.7, 187.3), turned to 90 degrees
- moved C1005 251.8 mm to (552.3, 197.5)
- moved R1009 251.6 mm to (559.6, 190.0), turned to 180 degrees
- moved C1003 249.6 mm to (557.1, 194.7)
- moved C1007 248.3 mm to (557.1, 197.7)
- moved L1001 247.2 mm to (539.2, 186.3)
- moved R1010 246.9 mm to (557.1, 196.2)
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
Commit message: Finished arranging groups of parts
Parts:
- removed BT1201: BR-2/3AE5SPN, Custom Footprints Library:BR-2_3AE5SPN
- C1203, C1207, C1801, C1802, C1803, C2101, C2102, C2103, C2104, C2105, C2106, C2107, C2108, D1801, Q1301, Q1304, Q1307, R1201, R1202, R1203, R1204, R1206, R1209, R1301, R1304, R1305, R1307, R1308, R1311, R1313, R1314, R1315, R1801, R1803, R1804, R2001, R2002, R2005, R2006, R2009, R2010, R2013, R605, R805: moved to B.Cu
- moved J1802 209.6 mm to (314.2, 176.7)
- moved J1801 204.5 mm to (325.9, 175.6)
- moved D2006 168.3 mm to (465.5, 211.3)
- moved U2006 167.4 mm to (462.3, 210.6)
- moved U2004 166.9 mm to (462.3, 206.2)
- moved U2002 165.0 mm to (462.3, 201.9)
- moved C2006 164.1 mm to (462.3, 212.7), turned to 180 degrees
- moved D2004 164.0 mm to (465.5, 207.0)
- moved R2010 158.9 mm to (462.3, 210.6), turned to 180 degrees
- moved R2012 158.8 mm to (465.5, 209.9)
- moved C2004 158.5 mm to (462.3, 208.4), turned to 180 degrees
- moved U2007 157.3 mm to (462.3, 197.6)
- moved D2002 157.0 mm to (465.5, 202.7)
- moved D2007 155.3 mm to (465.5, 198.4)
- moved C2002 154.7 mm to (462.3, 204.1), turned to 180 degrees
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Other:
- board text added: "+1.2VFF"
- board text added: "+12V"
- board text added: "+3.3V"
- board text added: "+5V"
- board text added: "+60VAN"
- board text added: "Analog Error"
- board text added: "CPU Trap"
- board text added: "Heart Beat"
- board text added: "I2C Error"
- board text added: "Low Batt"
- board text added: "Other Error"
- board text added: "PGOOD"
- board text added: "Reset/ Prog"
- board text added: "USB Error"

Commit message: placed most parts on board
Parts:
- added REF**: Symbol_Barrel_Polarity, Symbol:Symbol_Barrel_Polarity, F.Cu at (39.2, 76.2)
- C1004, C1006, C1008, C1104, C1105, D201, L1702, Q1501, R1003, R1004, R1005, R1009, R1501, R1503, R1505, R2203, R2903, U1001, U1103: moved to B.Cu
- moved C2002 347.0 mm to (138.2, 80.1)
- moved D2002 347.0 mm to (141.4, 78.7)
- moved R2002 347.0 mm to (138.2, 78.0)
- moved R2004 347.0 mm to (141.4, 77.3)
- moved U2002 347.0 mm to (138.2, 78.0)
- moved C2001 344.0 mm to (138.2, 71.4)
- moved C2003 344.0 mm to (138.2, 75.8)
- moved D2001 344.0 mm to (141.5, 70.0)
- moved D2003 344.0 mm to (141.4, 74.4)
- moved R2001 344.0 mm to (138.2, 69.3)
- moved R2003 344.0 mm to (141.5, 68.6)
- moved R2005 344.0 mm to (138.2, 73.6)
- moved R2007 344.0 mm to (141.4, 72.9)
- moved U2001 344.0 mm to (138.2, 69.3)
- moved U2003 344.0 mm to (138.2, 73.6)
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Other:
- board text added: "+"
- board text added: "+12VIN"
- board text added: "+5V_USB"
- board text added: "+5V_USB PGOOD"
- board text added: "-"
- board text added: "BLE UART"
- board text added: "GND"
- board text added: "GND_USB"
- board text added: "I2C"
- board text added: "MRST"
- board text added: "RX"
- board text added: "SCL"
- board text added: "SDA"
- board text added: "TX"
- board text added: "USB UART"

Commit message: Started routing
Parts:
- removed C2703, C2704: 0.1uF, Capacitors_SMD:C_0603
- removed D2701: Red, LEDs:LED_0603
- removed D2702: Yellow, LEDs:LED_0603
- removed R2705: 10k, Resistors_SMD:R_0603
- removed R2706, R2707: 1k, Resistors_SMD:R_0603
- removed U2702, U2703: 74LVC1G97, Package_TO_SOT_SMD:SOT-363_SC-70-6
- added G***: Heat_Caution_Symbol, Custom Footprints Library:Heat_Caution_Symbol, F.Cu at (131.5, 111.6)
- added G***: Microchip_Logo, Custom Footprints Library:Microchip_Logo, F.Cu at (195.9, 89.6)
- added G***: PIC32_Logo, Custom Footprints Library:PIC32_Logo, F.Cu at (208.8, 78.7)
- added TP1201: TP, Custom Footprints Library:Test_Point, F.Cu at (175.8, 100.3)
- added TP1202: TP, Custom Footprints Library:Test_Point, F.Cu at (187.4, 112.8)
- C2105, C2201, C2202, C2203, C2204, L1702, R2203, R2204, R2205: moved to F.Cu
- C2410, C2702, Q2701, R2701, R2702, R2703, R2704, U2105, U2201: moved to B.Cu
- TP1001, TP2401: footprint Measurement_Points:Measurement_Point_Round-SMD-Pad_Small -> Custom Footprints Library:Test_Point
- moved R2701 32.7 mm to (195.8, 107.5)
- moved R2702 29.8 mm to (195.8, 109.0)
- moved C2701 26.9 mm to (193.7, 114.4), turned to 270 degrees
- moved C2702 26.2 mm to (199.5, 114.9)
- moved Q2701 24.8 mm to (195.8, 111.4), turned to 270 degrees
- moved J1803 24.3 mm to (207.0, 100.8), turned to 90 degrees
- moved R2703 23.0 mm to (193.0, 108.6)
- moved U2701 22.9 mm to (198.9, 110.6)
- moved R2704 22.9 mm to (193.0, 110.2)
- moved C2101 11.2 mm to (77.6, 99.0)
- moved C2102 11.2 mm to (77.6, 100.6)
- moved U2101 11.2 mm to (77.6, 99.9)
- moved R1311 5.45 mm to (190.1, 108.5), turned to 180 degrees
- moved R2203 5.17 mm to (178.0, 95.1)
- moved L1702 4.94 mm to (178.1, 100.8), turned to 90 degrees
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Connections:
- J3001 pad 31: Anode_A_DSP -> Anode_DP_DSP
- J3001 pad 32: Grid_0_DSP -> Colon_1_DSP
- J3001 pad 33: Anode_B_DSP -> Anode_G_DSP
- J3001 pad 34: Grid_1_DSP -> Colon_0_DSP
- J3001 pad 35: Anode_C_DSP -> Anode_F_DSP
- J3001 pad 36: Grid_2_DSP -> Grid_5_DSP
- J3001 pad 37: Anode_D_DSP -> Anode_E_DSP
- J3001 pad 38: Grid_3_DSP -> Grid_4_DSP
- J3001 pad 39: Anode_E_DSP -> Anode_D_DSP
- J3001 pad 40: Grid_4_DSP -> Grid_3_DSP
- J3001 pad 41: Anode_F_DSP -> Anode_C_DSP
- J3001 pad 42: Grid_5_DSP -> Grid_2_DSP
- J3001 pad 43: Anode_G_DSP -> Anode_B_DSP
- J3001 pad 44: Colon_0_DSP -> Grid_1_DSP
- J3001 pad 45: Anode_DP_DSP -> Anode_A_DSP
- J3001 pad 46: Colon_1_DSP -> Grid_0_DSP
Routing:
- net GND: track 0.00 -> 141.7 mm, vias 0 -> 55
- net +3V3: track 0.00 -> 65.7 mm, vias 0 -> 17
- net +3.3V_BCKP: track 0.00 -> 50.1 mm, vias 0 -> 10
- net +5V_USB: track 0.00 -> 11.0 mm, vias 0 -> 3
- net MCU_SOSC: track 0.00 -> 8.54 mm, vias 0 -> 1
- net Net-(C1702-Pad1): track 0.00 -> 8.03 mm
- net GND_USB: track 0.00 -> 7.99 mm, vias 0 -> 2
- net Net-(R2911-Pad2): track 0.00 -> 7.93 mm, vias 0 -> 2
- net Net-(C1701-Pad1): track 0.00 -> 7.34 mm
- net GNDA: track 0.00 -> 7.02 mm
- net +3.3VA: track 0.00 -> 7.01 mm
- net Net-(C401-Pad1): track 0.00 -> 6.97 mm
- net Net-(R2912-Pad2): track 0.00 -> 6.94 mm, vias 0 -> 2
- net MCU_POSC_Enable: track 0.00 -> 6.39 mm, vias 0 -> 1
- net +5V: track 0.00 -> 6.23 mm, vias 0 -> 2
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- added copper zone on GND, net (none)
- added copper zone on PWR, net +3V3
- added copper zone on PWR, net +5V_USB
- added copper zone on GND, net GND
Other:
- copper layers 4 -> 6
- net class Default: trace_width 0.127 -> 0.254; via_dia 0.56 -> 0.4318
- net class Power: via_dia 0.56 -> 0.4318
- net class Signal: trace_width 0.127 -> 0.254; via_dia 0.56 -> 0.4318
- board text added: "+3.3V_BCKP"
- board text added: "+5V USB PGOOD"
- board text added: "PICKIT3"
- board text added: "USB COM"
- board text added: "USB COM Port: 115200 bps 8 bit data length No parity 1 stop bit No flow control"
- board text added: "VBAT"
- board text removed: "+5V_USB PGOOD"
- board text removed: "BLE Active"
- board text removed: "BLE Enable"

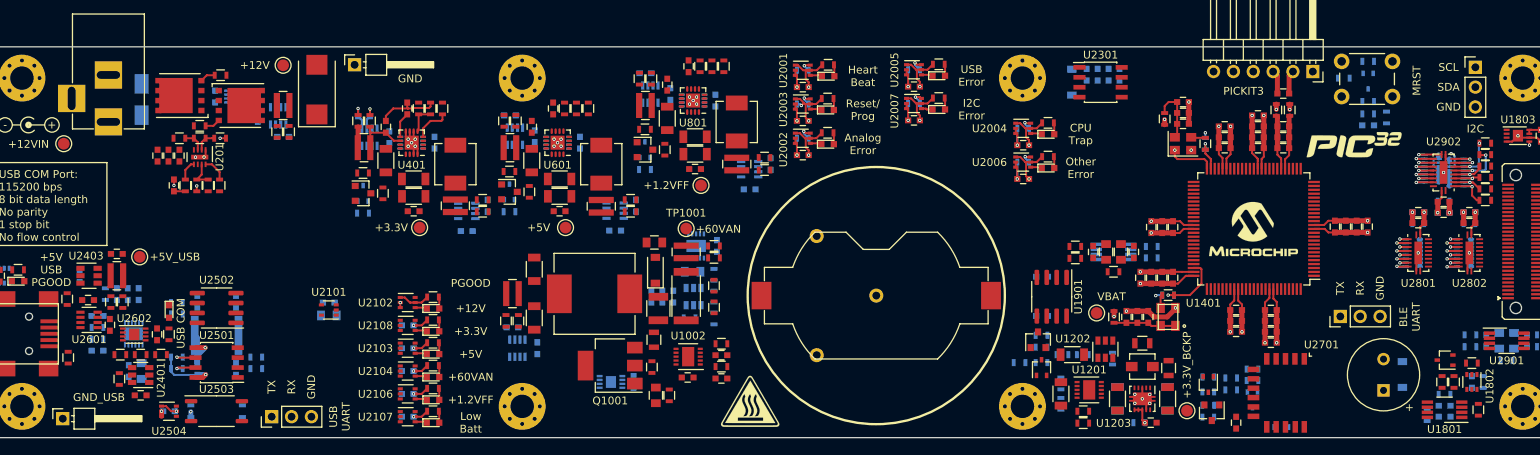
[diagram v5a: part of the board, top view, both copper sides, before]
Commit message: Lots more routing, primarily power stuff
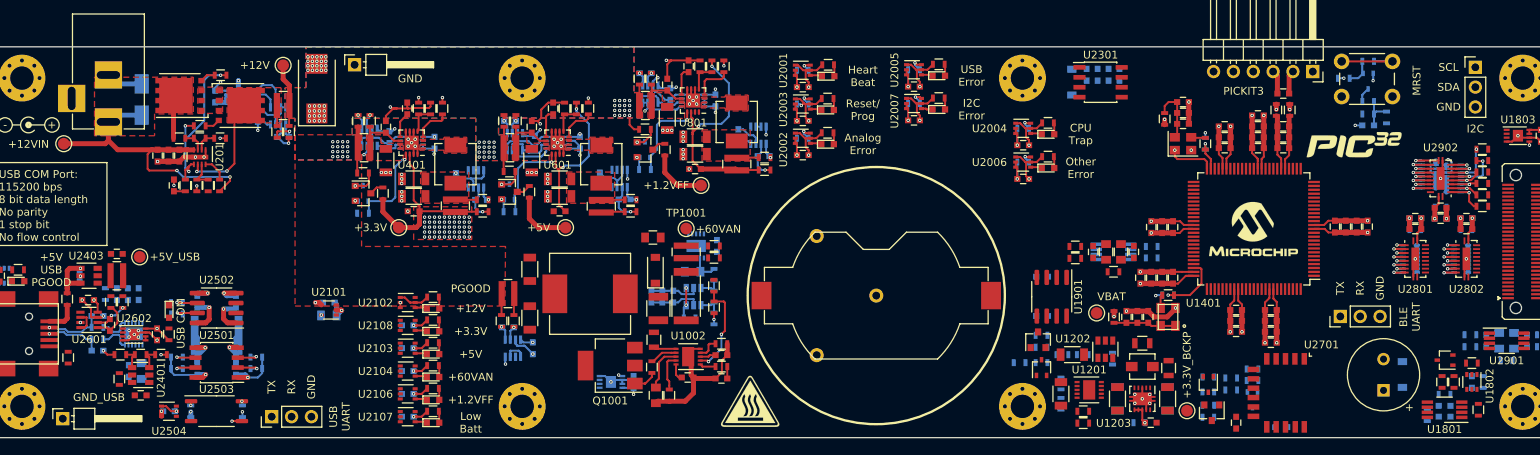
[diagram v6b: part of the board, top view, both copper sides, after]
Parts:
- removed C501: 0.1uF, Capacitors_SMD:C_0603
- moved C905 7.07 mm to (130.0, 77.6), turned to 90 degrees
- moved C705 6.95 mm to (112.3, 83.1), turned to 90 degrees
- moved C505 6.81 mm to (93.9, 83.2), turned to 90 degrees
- moved U903 4.48 mm to (132.6, 77.6), turned to 90 degrees
- moved U503 4.26 mm to (96.4, 83.2), turned to 90 degrees
- moved U703 4.17 mm to (114.8, 83.1), turned to 90 degrees
- moved TP401 2.67 mm to (86.6, 89.4)
- moved C704 1.68 mm to (115.4, 85.8), turned to 180 degrees
- moved C904 1.35 mm to (133.2, 80.3), turned to 180 degrees
- moved C504 1.12 mm to (97.1, 85.9), turned to 180 degrees
- moved C2801 0.85 mm to (216.6, 88.2)
- moved C2802 0.85 mm to (223.1, 88.2)
- moved C2803 0.85 mm to (216.6, 88.2)
- moved C2804 0.85 mm to (223.1, 88.2)
- moved C2805 0.85 mm to (216.6, 89.6)
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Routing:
- net GND: track 141.7 -> 302.4 mm, vias 55 -> 127
- net +3V3: track 65.7 -> 151.0 mm, vias 17 -> 90
- net +12Vin: track 0.00 -> 45.9 mm, vias 0 -> 2
- net +1.2VFF: track 0.00 -> 36.6 mm, vias 0 -> 2
- net +5V: track 6.23 -> 37.1 mm, vias 2 -> 4
- net +12V: track 2.69 -> 29.8 mm, vias 0 -> 65
- net I2C_SCL: track 0.00 -> 23.8 mm
- net Net-(R205-Pad1): track 2.62 -> 22.0 mm, vias 0 -> 3
- net I2C_SDA: track 0.00 -> 17.3 mm
- net Net-(Q202-Pad5): track 0.00 -> 15.2 mm, vias 0 -> 2
- net GND_USB: track 7.99 -> 22.7 mm, vias 2 -> 14
- net Net-(R1017-Pad2): track 0.00 -> 12.3 mm, vias 0 -> 2
- net POS3P3_RUN: track 0.00 -> 11.5 mm, vias 0 -> 1
- net POS5_RUN: track 0.00 -> 11.4 mm, vias 0 -> 1
- net +5V_USB: track 11.0 -> 22.4 mm, vias 3 -> 7
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- added copper zone on B.Cu, net +12V
- added copper zone on F.Cu, net +12V
- added copper zone on F.Cu, net +12Vin
- added copper zone on F.Cu, net +3V3
- added copper zone on F.Cu, net Net-(C401-Pad1)
- added copper zone on F.Cu, net Net-(C404-Pad1)
- added copper zone on F.Cu, net Net-(C601-Pad1)
- added copper zone on F.Cu, net Net-(C604-Pad1)
- added copper zone on F.Cu, net Net-(C801-Pad1)
- added copper zone on F.Cu, net Net-(C804-Pad1)
- added copper zone on F.Cu, net Net-(L401-Pad1)
- added copper zone on F.Cu, net Net-(L601-Pad1)
- added copper zone on F.Cu, net Net-(L801-Pad1)
- added copper zone on F.Cu, net Net-(Q201-Pad1)
- added copper zone on F.Cu, net Net-(Q202-Pad5)

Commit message: More routing
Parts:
- moved TP2401 0.57 mm to (53.4, 92.6)
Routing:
- net POS5_USB_PGOOD: track 0.00 -> 37.8 mm, vias 0 -> 3
- net +5V_USB: track 22.4 -> 56.0 mm, vias 7 -> 24
- net I2C_USB_SCL: track 3.38 -> 29.9 mm, vias 1 -> 2
- net Net-(J2401-Pad6): track 0.00 -> 22.7 mm
- net USB_UART_TX_ISO: track 3.16 -> 24.6 mm, vias 1 -> 2
- net GND: track 302.4 -> 317.6 mm, vias 127 -> 134
- net I2C_USB_SDA: track 6.01 -> 21.0 mm
- net /USB UART Bridge/CONN_USB+: track 7.33 -> 22.2 mm, vias 1 -> 2
- net Net-(C2102-Pad1): track 4.00 -> 17.1 mm
- net GND_USB: track 22.7 -> 33.9 mm, vias 14 -> 27
- net USB_UART_RX: track 3.31 -> 12.8 mm
- net USB_UART_TX: track 3.21 -> 12.4 mm
- net USB_UART_RX_ISO: track 3.18 -> 9.87 mm, vias 1 -> 2
- net Net-(D2104-Pad1): track 0.00 -> 6.36 mm, vias 0 -> 1
- net /USB UART Bridge/CONN_USB-: track 7.33 -> 13.0 mm, vias 1 -> 2
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- added copper zone on F.Cu, net +5V_USB
- added copper zone on F.Cu, net GND_USB
- added copper zone on GND, net GND_USB
- added copper zone on F.Cu, net Net-(C1001-Pad1)
- added copper zone on F.Cu, net Net-(D1001-Pad2)
- removed copper zone on GND, net (none)

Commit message: Moar routing
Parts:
- moved C2806 8.96 mm to (214.4, 87.4)
- moved R2802 8.96 mm to (214.4, 87.5)
- moved U2802 8.96 mm to (214.4, 91.2)
- moved C2802 8.96 mm to (214.4, 86.0)
- moved C2804 8.96 mm to (214.4, 86.0)
- moved RN2802 8.96 mm to (213.7, 91.2)
- moved C2805 6.06 mm to (221.6, 86.1)
- moved R2801 6.06 mm to (221.6, 86.2)
- moved RN2801 6.06 mm to (220.9, 89.9)
- moved U2801 6.06 mm to (221.6, 89.9)
- moved C2801 6.06 mm to (221.6, 84.7)
- moved C2803 6.06 mm to (221.6, 84.7)
- moved RN2902 2.47 mm to (220.3, 81.0)
- moved C2901 2.47 mm to (218.6, 86.1)
- moved C2902 2.47 mm to (218.6, 86.1)
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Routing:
- net I2C_SDA: track 17.3 -> 121.3 mm, vias 0 -> 5
- net I2C_SCL: track 24.0 -> 121.6 mm, vias 0 -> 9
- net GND: track 317.6 -> 377.8 mm, vias 134 -> 201
- net +3V3: track 153.6 -> 204.9 mm, vias 90 -> 111
- net Net-(BT1202-Pad1): track 0.00 -> 35.8 mm
- net ~MCLR: track 0.00 -> 28.6 mm, vias 0 -> 1
- net Grid_0_DSP: track 0.00 -> 22.5 mm, vias 0 -> 2
- net Grid_1_DSP: track 0.00 -> 22.4 mm, vias 0 -> 2
- net Grid_2_DSP: track 0.00 -> 22.2 mm, vias 0 -> 2
- net Grid_3_DSP: track 0.00 -> 22.0 mm, vias 0 -> 2
- net VBAT: track 0.00 -> 22.0 mm, vias 0 -> 3
- net Grid_4_DSP: track 0.00 -> 21.8 mm, vias 0 -> 2
- net +60VAN: track 6.48 -> 28.1 mm, vias 0 -> 1
- net Colon_1_DSP: track 0.00 -> 21.5 mm, vias 0 -> 2
- net Grid_5_DSP: track 0.00 -> 21.4 mm, vias 0 -> 2
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- added copper zone on F.Cu, net GND
- added copper zone on F.Cu, net Net-(C1010-Pad1)
- added copper zone on F.Cu, net Net-(L1201-Pad1)
- added copper zone on F.Cu, net Net-(L1201-Pad2)
